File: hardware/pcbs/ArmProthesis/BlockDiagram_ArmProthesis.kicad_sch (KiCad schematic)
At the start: 4 parts

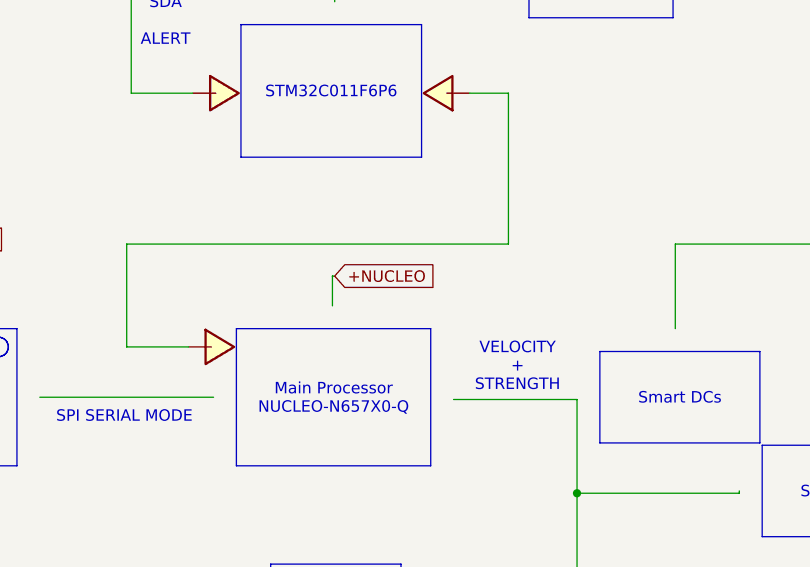
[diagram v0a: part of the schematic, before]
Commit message: Voltage supply of sEMG & ADC
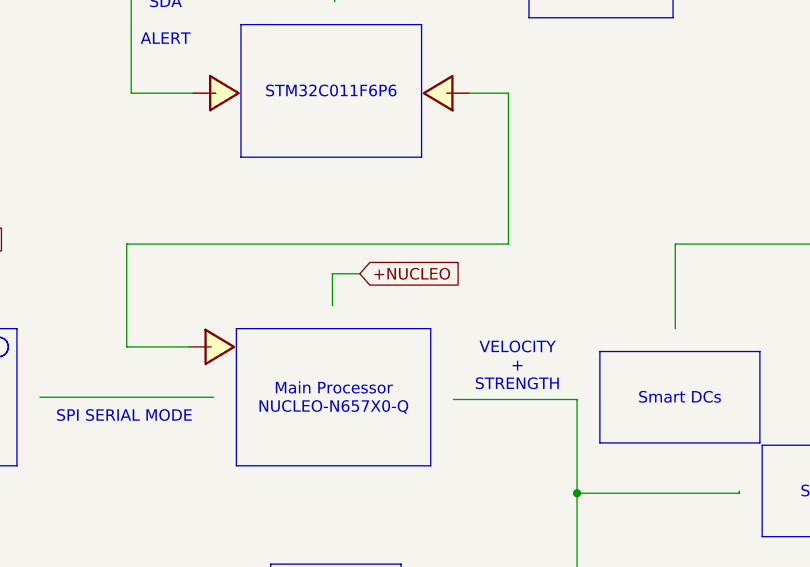
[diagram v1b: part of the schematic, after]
